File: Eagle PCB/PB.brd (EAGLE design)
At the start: 43.6 x 39.1 mm, 25 parts, among them IC1 74HC595D, IC2 74HC595D, IC3 L78LXXCU/BU, J1 61300511121, J2 61300211121, J3 61300211121, J4 61300511121, J5 61300211121, J6 61300511121, J7 61300211121

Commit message: Final PCB schematic and board added.
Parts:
- removed J3, J5: 61300211121, Headers:61300211121
- added JP1, JP2, JP3, JP4, JP5, JP6: (no value), pinhead:1X01
- moved R3 30.4 mm to (43.9, 5.97)
- moved C9 29.2 mm to (39.4, 16.6)
- moved C2 28.3 mm to (3.05, 9.65)
- moved DRV8833PWP1 28.1 mm to (7.49, 9.65)
- moved J1 27.9 mm to (7.87, 2.67)
- moved J6 27.9 mm to (36.1, 2.67)
- moved C8 27.1 mm to (31.6, 9.78)
- moved DRV8833PWP3 27.0 mm to (35.8, 9.65)
- moved C3 25.8 mm to (11.0, 16.5)
- moved R1 25.5 mm to (15.1, 6.22)
- moved J2 14.1 mm to (23.5, 32.5)
- moved C1 7.01 mm to (8.26, 16.4), turned to 90 degrees
- moved C4 6.51 mm to (22.5, 16.5), turned to 90 degrees
- moved C7 6.21 mm to (36.6, 16.6), turned to 90 degrees
- moved J7 3.94 mm to (2.67, 16.4)
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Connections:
- net N$11 renamed SA
- removed net GND: IC1.8, IC2.8, IC3.4
- removed net N$1: IC1.12, J2.2
- removed net N$12: IC2.14, J3.1
- removed net N$25: IC2.12, J3.2
- new net OE: IC1.13, IC2.13, JP1.1, JP4.1
- new net RCK: IC1.12, IC2.12, JP2.1, JP5.1
- new net SB: IC2.14, J2.2
- net 0: now also IC1.8, IC2.8, IC3.4; no longer IC1.13, IC2.13, J5.2
- net CLK: now also JP3.1, JP6.1
- net VCC: no longer J5.1
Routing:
- net VDD: track 165.0 -> 92.5 mm, vias 10 -> 9
- net OE: track 0.00 -> 60.0 mm, vias 0 -> 4
- net 0: track 108.1 -> 52.1 mm, vias 9 -> 10
- net RCK: track 0.00 -> 53.3 mm, vias 0 -> 2
- net CLK: track 27.5 -> 63.3 mm
- net B1: track 42.7 -> 13.0 mm, vias 4 -> 2
- net E2: track 37.6 -> 11.3 mm, vias 2 -> 0
- net A1: track 53.6 -> 28.3 mm
- net F1: track 9.89 -> 33.8 mm
- net E1: track 11.0 -> 29.5 mm
- net SA: track 3.99 -> 18.3 mm
- net SB: track 0.00 -> 13.3 mm
- net N$2: track 16.8 -> 4.87 mm
- net F2: track 29.1 -> 18.3 mm, vias 2 -> 0
- net N$21: track 12.1 -> 4.45 mm
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- added copper zone on layer 16, net 0
- added copper zone on layer 1, net VDD
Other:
- board size 43.6 x 39.1 mm -> 46.5 x 36.6 mm
- board text added: "(c) 2020-2021"
- board text added: "78L05"
- board text added: "A1"
- board text added: "A2"
- board text added: "B1"
- board text added: "B2"
- board text added: "C1"
- board text added: "C2"
- board text added: "CLK"
- board text added: "D1"
- board text added: "D2"
- board text added: "DRV8833"
- board text added: "E1"
- board text added: "E2"
- board text added: "F1"
- board text added: "F2"
- board text added: "GND"
- board text added: "OE"
- board text added: "PORTABLE BRAILLE v 2.0"
- board text added: "RCLK"
- board text added: "SERA"
- board text added: "SERB"
- board text added: "Spider.RAR"
- board text added: "ULT"
- board text added: "VDD"

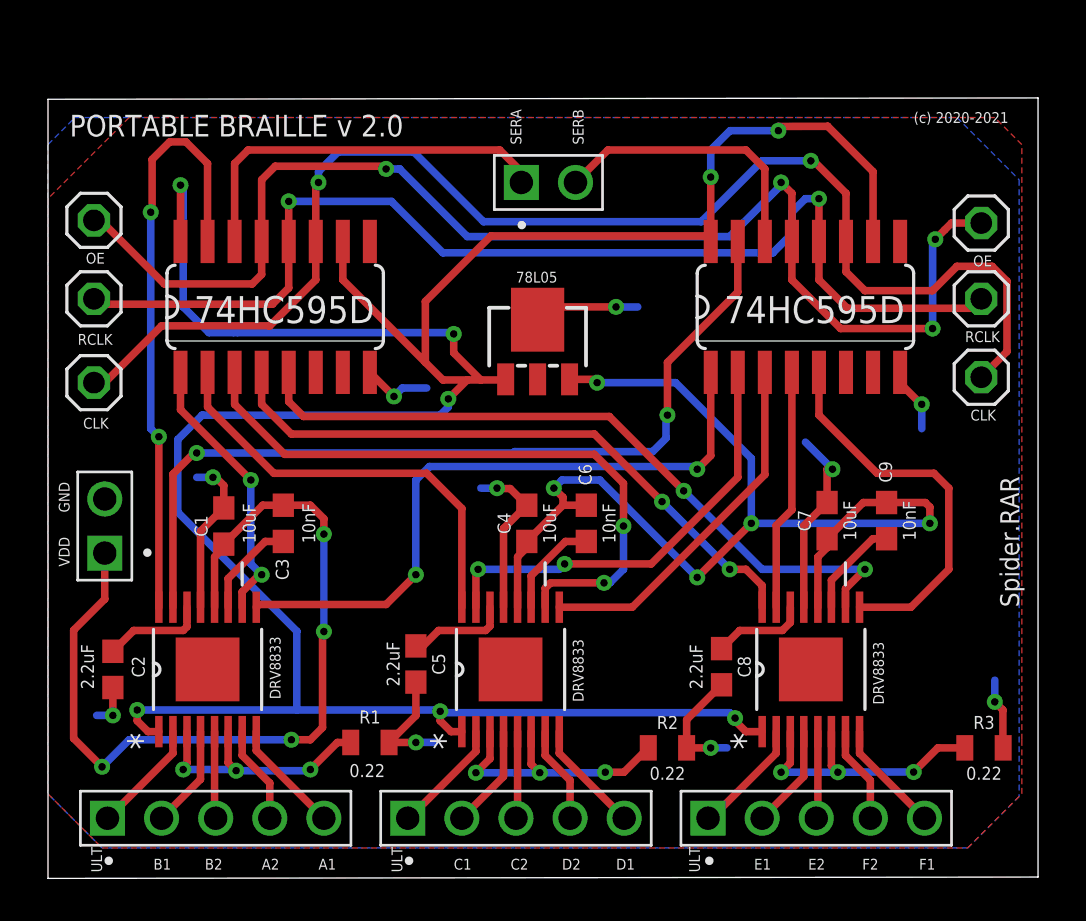
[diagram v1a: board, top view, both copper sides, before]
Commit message: PCB updated with common serial input.
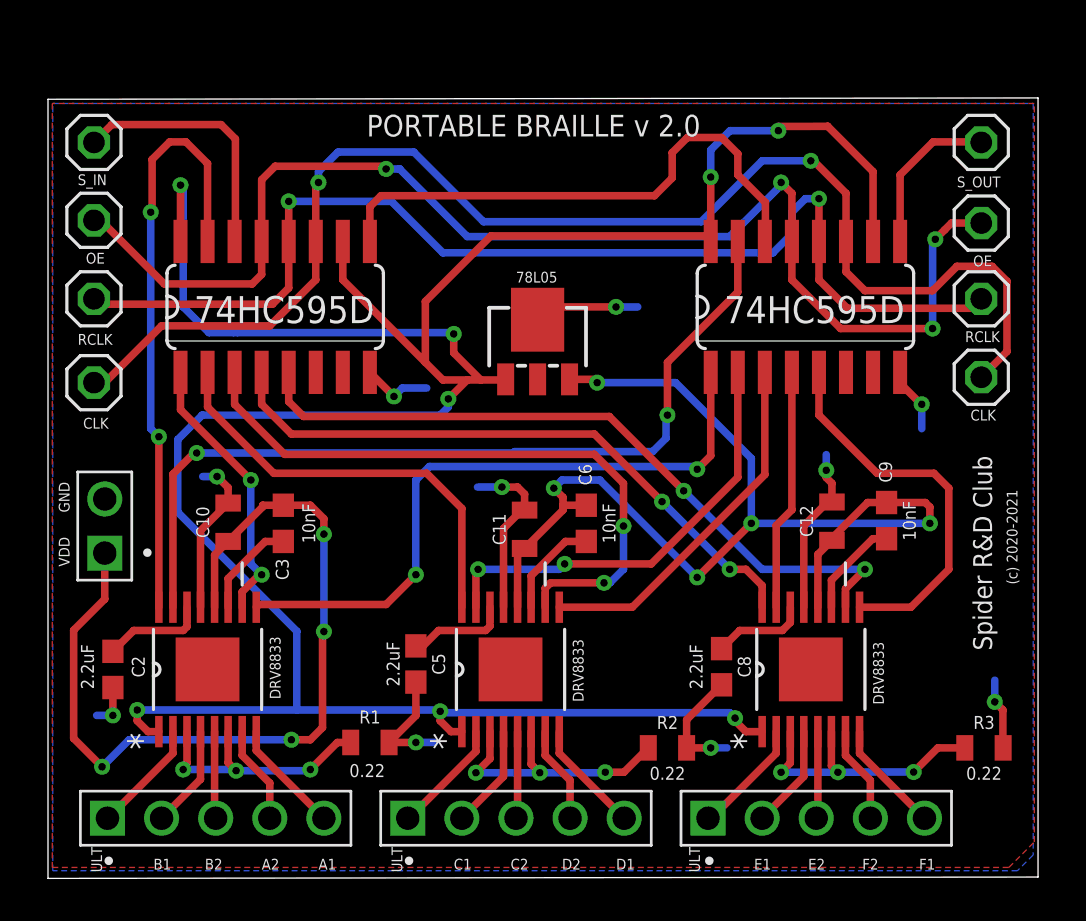
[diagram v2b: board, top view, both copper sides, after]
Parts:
- removed C1, C4, C7: 10uF, SparkFun-Capacitors:0603
- removed J2: 61300211121, Headers:61300211121
- added C10, C11, C12: 10uF, SparkFun-Capacitors:0805
- added JP7, JP8: (no value), pinhead:1X01
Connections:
- new net N$1: IC2.9, JP8.1
- net 0: now also C10.2, C11.2, C12.2; no longer C1.2, C4.2, C7.2
- net SA: now also JP7.1; no longer J2.1
- net SB: now also IC1.9; no longer J2.2
- net VDD: now also C10.1, C11.1, C12.1; no longer C1.1, C4.1, C7.1
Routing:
- net SB: track 13.3 -> 25.9 mm
- net N$1: track 0.00 -> 7.59 mm
- net SA: track 18.3 -> 12.1 mm
- net 0: track 52.1 -> 51.4 mm
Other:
- board text added: "S_IN"
- board text added: "S_OUT"
- board text added: "Spider R&D Club"
- board text removed: "SERA"
- board text removed: "SERB"
- board text removed: "Spider.RAR"
